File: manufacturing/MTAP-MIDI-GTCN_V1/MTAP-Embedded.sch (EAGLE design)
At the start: 61 parts, among them J1 629105150521, X10 0R, X11 0R

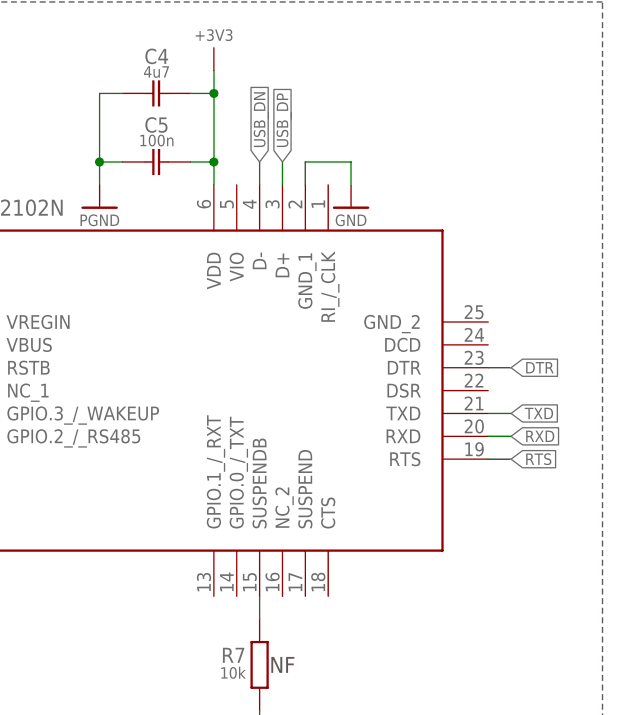
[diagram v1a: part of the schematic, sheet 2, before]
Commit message: Finalised Board
added missing connections to USB Bridge.
Added 3d Images to docs
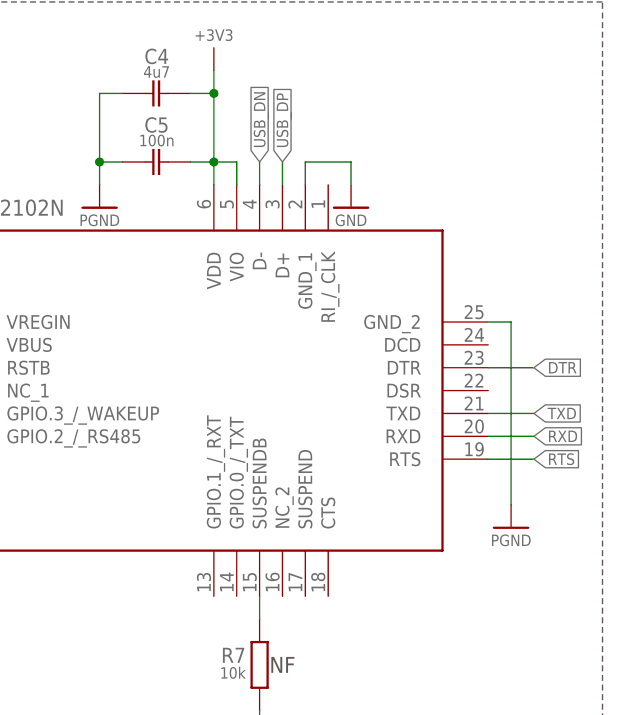
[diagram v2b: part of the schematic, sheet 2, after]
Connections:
- net +3V3: now also D2.VIO
- net PGND: now also D2.GND_2
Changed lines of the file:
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@@
 <part name="SPI_CLK" library="solpad_GruS" library_urn="urn:adsk.eagle:library:13571267" deviceset="SMD-TP" device="" package3d_urn="urn:adsk.eagle:package:38312116/4"/>
 <part name="S1" library="switch_GruS" library_urn="urn:adsk.eagle:library:13571161" deviceset="TASTE10XX" device="WE" package3d_urn="urn:adsk.eagle:package:18368072/4" value="BOOT"/>
+<part name="PGND5" library="supply_GruS" library_urn="urn:adsk.eagle:library:13579815" deviceset="PGND" device=""/>
 </parts>
 <sheets>
@@
 <attribute name="VALUE" x="78.74" y="91.44" size="1.27" layer="96" font="vector" align="bottom-center"/>
 </instance>
+<instance part="PGND5" gate="G$1" x="162.56" y="208.28" smashed="yes">
+<attribute name="VALUE" x="162.56" y="206.248" size="1.27" layer="96" font="vector" align="bottom-center"/>
+</instance>
 </instances>
 <busses>
@@
 </segment>
 <segment>
+<pinref part="GND1" gate="1" pin="GND"/>
+<wire x1="144.78" y1="248.92" x2="144.78" y2="246.38" width="0.1524" layer="91"/>
+<wire x1="139.7" y1="248.92" x2="144.78" y2="248.92" width="0.1524" layer="91"/>
 <wire x1="139.7" y1="246.38" x2="139.7" y2="248.92" width="0.1524" layer="91"/>
-<wire x1="139.7" y1="248.92" x2="144.78" y2="248.92" width="0.1524" layer="91"/>
-<wire x1="144.78" y1="248.92" x2="144.78" y2="246.38" width="0.1524" layer="91"/>
-<pinref part="GND1" gate="1" pin="GND"/>
 <pinref part="D2" gate="G$1" pin="GND_1"/>
 </segment>
@@
 </segment>
 <segment>
-<wire x1="160.02" y1="220.98" x2="162.56" y2="220.98" width="0.1524" layer="91"/>
-<label x="162.56" y="220.98" size="1.27" layer="95" xref="yes"/>
+<wire x1="160.02" y1="220.98" x2="165.1" y2="220.98" width="0.1524" layer="91"/>
+<label x="165.1" y="220.98" size="1.27" layer="95" xref="yes"/>
 <pinref part="D2" gate="G$1" pin="TXD"/>
 </segment>
@@
 </segment>
 <segment>
-<wire x1="160.02" y1="218.44" x2="162.56" y2="218.44" width="0.1524" layer="91"/>
-<label x="162.56" y="218.44" size="1.27" layer="95" xref="yes"/>
+<wire x1="160.02" y1="218.44" x2="165.1" y2="218.44" width="0.1524" layer="91"/>
+<label x="165.1" y="218.44" size="1.27" layer="95" xref="yes"/>
 <pinref part="D2" gate="G$1" pin="RXD"/>
 </segment>
@@
 </segment>
 <segment>
-<wire x1="160.02" y1="226.06" x2="162.56" y2="226.06" width="0.1524" layer="91"/>
-<label x="162.56" y="226.06" size="1.27" layer="95" xref="yes"/>
+<wire x1="160.02" y1="226.06" x2="165.1" y2="226.06" width="0.1524" layer="91"/>
+<label x="165.1" y="226.06" size="1.27" layer="95" xref="yes"/>
 <pinref part="D2" gate="G$1" pin="DTR"/>
 </segment>
@@
 </segment>
 <segment>
-<wire x1="160.02" y1="215.9" x2="162.56" y2="215.9" width="0.1524" layer="91"/>
-<label x="162.56" y="215.9" size="1.27" layer="95" xref="yes"/>
+<wire x1="160.02" y1="215.9" x2="165.1" y2="215.9" width="0.1524" layer="91"/>
+<label x="165.1" y="215.9" size="1.27" layer="95" xref="yes"/>
 <pinref part="D2" gate="G$1" pin="RTS"/>
 </segment>
@@
 <wire x1="129.54" y1="259.08" x2="129.54" y2="256.54" width="0.1524" layer="91"/>
 <junction x="129.54" y="256.54"/>
+<pinref part="D2" gate="G$1" pin="VIO"/>
+<wire x1="132.08" y1="246.38" x2="132.08" y2="248.92" width="0.1524" layer="91"/>
+<wire x1="132.08" y1="248.92" x2="129.54" y2="248.92" width="0.1524" layer="91"/>
 </segment>
 </net>
@@
 <junction x="116.84" y="248.92"/>
 </segment>
-</net>
+<segment>
+<pinref part="D2" gate="G$1" pin="GND_2"/>
+<wire x1="160.02" y1="231.14" x2="162.56" y2="231.14" width="0.1524" layer="91"/>
+<wire x1="162.56" y1="231.14" x2="162.56" y2="210.82" width="0.1524" layer="91"/>
+<pinref part="PGND5" gate="G$1" pin="PGND"/>
+</segment>
+</net>

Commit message: midi functional test
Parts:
- added C19: 1u, rcl_GruS:C-EUC0805
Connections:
- net AGND: now also C19.2
- net AINP: now also C19.1, D1.IO4
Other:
- note added: "G6 Filter (~1500Hz) 2.8V/V Gain Sallen Key Aufbau Butterworth Charakeristik Single Supply"
- note removed: "A6 Filter (1760Hz) 2V/V Gain Sallen Key Aufbau Butterworth Charakeristik Single Supply"
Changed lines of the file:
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@@
 <part name="S1" library="switch_GruS" library_urn="urn:adsk.eagle:library:13571161" deviceset="TASTE10XX" device="WE" package3d_urn="urn:adsk.eagle:package:18368072/4" value="BOOT"/>
 <part name="PGND5" library="supply_GruS" library_urn="urn:adsk.eagle:library:13579815" deviceset="PGND" device=""/>
+<part name="C19" library="rcl_GruS" library_urn="urn:adsk.eagle:library:13572313" deviceset="C-EU" device="C0805" package3d_urn="urn:adsk.eagle:package:23617/2" value="1u"/>
+<part name="AGND13" library="supply_GruS" library_urn="urn:adsk.eagle:library:13579815" deviceset="AGND" device=""/>
 </parts>
 <sheets>
@@
 <instance part="SPIQ" gate="G$1" x="114.3" y="114.3" smashed="yes"/>
 <instance part="SPI_CLK" gate="G$1" x="119.38" y="114.3" smashed="yes"/>
+<instance part="C19" gate="G$1" x="129.54" y="157.48" smashed="yes">
+<attribute name="NAME" x="128.778" y="156.9466" size="1.6764" layer="95" font="vector" align="bottom-right"/>
+<attribute name="VALUE" x="128.524" y="154.1526" size="1.27" layer="96" font="vector" align="bottom-right"/>
+</instance>
+<instance part="AGND13" gate="G$1" x="129.54" y="147.32" smashed="yes">
+<attribute name="VALUE" x="129.54" y="145.288" size="1.27" layer="96" font="vector" align="bottom-center"/>
+</instance>
 </instances>
 <busses>
@@
 <pinref part="D1" gate="G$1" pin="GND_1"/>
 <wire x1="81.28" y1="210.82" x2="83.82" y2="210.82" width="0.1524" layer="91"/>
+</segment>
+<segment>
+<pinref part="GND8" gate="1" pin="GND"/>
+<pinref part="C3" gate="G$1" pin="2"/>
+<wire x1="55.88" y1="149.86" x2="55.88" y2="152.4" width="0.1524" layer="91"/>
 </segment>
 <segment>
@@
 <pinref part="GND7" gate="1" pin="GND"/>
 </segment>
-<segment>
-<pinref part="GND8" gate="1" pin="GND"/>
-<pinref part="C3" gate="G$1" pin="2"/>
-<wire x1="55.88" y1="149.86" x2="55.88" y2="152.4" width="0.1524" layer="91"/>
-</segment>
 </net>
 <net name="GPIO0" class="0">
 <segment>
 <pinref part="D1" gate="G$1" pin="IO0"/>
-<wire x1="121.92" y1="210.82" x2="124.46" y2="210.82" width="0.1524" layer="91"/>
-<label x="124.46" y="210.82" size="1.27" layer="95" xref="yes"/>
+<wire x1="121.92" y1="210.82" x2="127" y2="210.82" width="0.1524" layer="91"/>
+<label x="127" y="210.82" size="1.27" layer="95" xref="yes"/>
 </segment>
 </net>
@@
 <segment>
 <pinref part="D1" gate="G$1" pin="TXD0"/>
-<wire x1="121.92" y1="185.42" x2="124.46" y2="185.42" width="0.1524" layer="91"/>
-<label x="124.46" y="185.42" size="1.27" layer="95" xref="yes"/>
+<wire x1="121.92" y1="185.42" x2="127" y2="185.42" width="0.1524" layer="91"/>
+<label x="127" y="185.42" size="1.27" layer="95" xref="yes"/>
 </segment>
 </net>
@@
 <segment>
 <pinref part="D1" gate="G$1" pin="RXD0"/>
-<wire x1="121.92" y1="187.96" x2="124.46" y2="187.96" width="0.1524" layer="91"/>
-<label x="124.46" y="187.96" size="1.27" layer="95" xref="yes"/>
+<wire x1="121.92" y1="187.96" x2="127" y2="187.96" width="0.1524" layer="91"/>
+<label x="127" y="187.96" size="1.27" layer="95" xref="yes"/>
 </segment>
 </net>
@@
 <segment>
 <pinref part="D1" gate="G$1" pin="IO5"/>
-<wire x1="121.92" y1="200.66" x2="124.46" y2="200.66" width="0.1524" layer="91"/>
-<label x="124.46" y="200.66" size="1.27" layer="95" xref="yes"/>
+<wire x1="121.92" y1="200.66" x2="127" y2="200.66" width="0.1524" layer="91"/>
+<label x="127" y="200.66" size="1.27" layer="95" xref="yes"/>
 </segment>
 <segment>
@@
 <segment>
 <pinref part="D1" gate="G$1" pin="IO18"/>
-<wire x1="121.92" y1="198.12" x2="124.46" y2="198.12" width="0.1524" layer="91"/>
-<label x="124.46" y="198.12" size="1.27" layer="95" xref="yes"/>
+<wire x1="121.92" y1="198.12" x2="127" y2="198.12" width="0.1524" layer="91"/>
+<label x="127" y="198.12" size="1.27" layer="95" xref="yes"/>
 </segment>
 <segment>
@@
 <segment>
 <pinref part="D1" gate="G$1" pin="IO19"/>
-<wire x1="121.92" y1="195.58" x2="124.46" y2="195.58" width="0.1524" layer="91"/>
-<label x="124.46" y="195.58" size="1.27" layer="95" xref="yes"/>
+<wire x1="121.92" y1="195.58" x2="127" y2="195.58" width="0.1524" layer="91"/>
+<label x="127" y="195.58" size="1.27" layer="95" xref="yes"/>
 </segment>
 <segment>
@@
 <wire x1="73.66" y1="111.76" x2="73.66" y2="109.22" width="0.1524" layer="91"/>
 </segment>
+<segment>
+<pinref part="C19" gate="G$1" pin="2"/>
+<wire x1="129.54" y1="149.86" x2="129.54" y2="152.4" width="0.1524" layer="91"/>
+<pinref part="AGND13" gate="G$1" pin="AGND"/>
+</segment>
 </net>
 <net name="AINP" class="0">
@@
 <pinref part="POST-AFE" gate="G$1" pin="P$1"/>
 <wire x1="93.98" y1="111.76" x2="93.98" y2="109.22" width="0.1524" layer="91"/>
+</segment>
+<segment>
+<pinref part="C19" gate="G$1" pin="1"/>
+<wire x1="129.54" y1="160.02" x2="129.54" y2="180.34" width="0.1524" layer="91"/>
+<pinref part="D1" gate="G$1" pin="IO4"/>
+<wire x1="127" y1="208.28" x2="124.46" y2="208.28" width="0.1524" layer="91"/>
+<label x="127" y="208.28" size="1.27" layer="95" xref="yes"/>
+<wire x1="124.46" y1="208.28" x2="121.92" y2="208.28" width="0.1524" layer="91"/>
+<wire x1="129.54" y1="180.34" x2="124.46" y2="180.34" width="0.1524" layer="91"/>
+<wire x1="124.46" y1="180.34" x2="124.46" y2="208.28" width="0.1524" layer="91"/>
+<junction x="124.46" y="208.28"/>
 </segment>
 </net>
@@
 Supply and Reference</text>
 <text x="88.9" y="172.72" size="2.54" layer="97" font="vector" align="bottom-center">Low Pass Filter</text>
-<text x="162.56" y="116.84" size="1.778" layer="97" font="vector" rot="R180">A6 Filter (1760Hz)
-2V/V Gain
+<text x="162.56" y="116.84" size="1.778" layer="97" font="vector" rot="R180">G6 Filter (~1500Hz)
+2.8V/V Gain
 Sallen Key Aufbau
 Butterworth Charakeristik

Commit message: upd midi serial
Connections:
- new net MTDO: D1.IO15
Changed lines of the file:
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@@
+</segment>
+</net>
+<net name="MTDO" class="0">
+<segment>
+<pinref part="D1" gate="G$1" pin="IO15"/>
+<wire x1="83.82" y1="154.94" x2="78.74" y2="154.94" width="0.1524" layer="91"/>
+<label x="78.74" y="154.94" size="1.27" layer="95" rot="R180" xref="yes"/>
 </segment>
 </net>

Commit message: placed pcb order
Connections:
- net +3V3: now also N1.NC
- net GND: no longer D2.GND_1
- net PGND: now also D2.GND_1
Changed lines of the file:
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@@
 <part name="N2" library="opv_GruS" library_urn="urn:adsk.eagle:library:27826080" deviceset="TLV271C*" device="DBVTG4" package3d_urn="urn:adsk.eagle:package:38237664/3" value="TLV271G4"/>
 <part name="D2" library="ic_GruS" library_urn="urn:adsk.eagle:library:13571010" deviceset="CP2102N-A02-GQFN24" device="" package3d_urn="urn:adsk.eagle:package:38290199/3" value="CP2102N"/>
-<part name="GND1" library="supply_GruS" library_urn="urn:adsk.eagle:library:13579815" deviceset="GND" device=""/>
 <part name="+3V1" library="supply_GruS" library_urn="urn:adsk.eagle:library:13579815" deviceset="+3V3" device=""/>
 <part name="C5" library="rcl_GruS" library_urn="urn:adsk.eagle:library:13572313" deviceset="C-EU" device="C0805" package3d_urn="urn:adsk.eagle:package:23617/2" value="100n"/>
@@
 <part name="C19" library="rcl_GruS" library_urn="urn:adsk.eagle:library:13572313" deviceset="C-EU" device="C0805" package3d_urn="urn:adsk.eagle:package:23617/2" value="1u"/>
 <part name="AGND13" library="supply_GruS" library_urn="urn:adsk.eagle:library:13579815" deviceset="AGND" device=""/>
+<part name="+3V8" library="supply_GruS" library_urn="urn:adsk.eagle:library:13579815" deviceset="+3V3" device=""/>
+<part name="PGND18" library="supply_GruS" library_urn="urn:adsk.eagle:library:13579815" deviceset="PGND" device=""/>
 </parts>
 <sheets>
@@
 <attribute name="VALUE" x="102.87" y="243.84" size="1.778" layer="96" align="center-left"/>
 </instance>
-<instance part="GND1" gate="1" x="144.78" y="243.84" smashed="yes">
-<attribute name="VALUE" x="144.78" y="241.808" size="1.27" layer="96" font="vector" align="bottom-center"/>
-</instance>
 <instance part="+3V1" gate="G$1" x="129.54" y="261.62" smashed="yes">
 <attribute name="VALUE" x="129.54" y="262.382" size="1.27" layer="96" font="vector" align="bottom-center"/>
@@
 <instance part="PGND5" gate="G$1" x="162.56" y="208.28" smashed="yes">
 <attribute name="VALUE" x="162.56" y="206.248" size="1.27" layer="96" font="vector" align="bottom-center"/>
+</instance>
+<instance part="+3V8" gate="G$1" x="101.6" y="157.48" smashed="yes">
+<attribute name="VALUE" x="101.6" y="158.242" size="1.27" layer="96" font="vector" align="bottom-center"/>
+</instance>
+<instance part="PGND18" gate="G$1" x="144.78" y="243.84" smashed="yes">
+<attribute name="VALUE" x="144.78" y="241.808" size="1.27" layer="96" font="vector" align="bottom-center"/>
 </instance>
 </instances>
@@
 <wire x1="139.7" y1="91.44" x2="139.7" y2="81.28" width="0.1524" layer="91"/>
 <pinref part="GND2" gate="1" pin="GND"/>
-</segment>
-<segment>
-<pinref part="GND1" gate="1" pin="GND"/>
-<wire x1="144.78" y1="248.92" x2="144.78" y2="246.38" width="0.1524" layer="91"/>
-<wire x1="139.7" y1="248.92" x2="144.78" y2="248.92" width="0.1524" layer="91"/>
-<wire x1="139.7" y1="246.38" x2="139.7" y2="248.92" width="0.1524" layer="91"/>
-<pinref part="D2" gate="G$1" pin="GND_1"/>
 </segment>
 </net>
@@
 <pinref part="V2" gate="G$1" pin="E"/>
 <wire x1="58.42" y1="208.28" x2="58.42" y2="210.82" width="0.1524" layer="91"/>
-<wire x1="58.42" y1="210.82" x2="33.02" y2="210.82" width="0.1524" layer="91"/>
-<wire x1="33.02" y1="210.82" x2="33.02" y2="220.98" width="0.1524" layer="91"/>
+<wire x1="58.42" y1="210.82" x2="43.18" y2="210.82" width="0.1524" layer="91"/>
 <pinref part="R4" gate="G$1" pin="1"/>
-<wire x1="33.02" y1="220.98" x2="38.1" y2="220.98" width="0.1524" layer="91"/>
-<wire x1="33.02" y1="220.98" x2="30.48" y2="220.98" width="0.1524" layer="91"/>
-<junction x="33.02" y="220.98"/>
-<label x="30.48" y="220.98" size="1.27" layer="95" font="vector" rot="R180" xref="yes"/>
+<wire x1="35.56" y1="220.98" x2="38.1" y2="220.98" width="0.1524" layer="91"/>
+<wire x1="35.56" y1="220.98" x2="33.02" y2="220.98" width="0.1524" layer="91"/>
+<label x="33.02" y="220.98" size="1.27" layer="95" font="vector" rot="R180" xref="yes"/>
+<wire x1="35.56" y1="220.98" x2="35.56" y2="218.44" width="0.1524" layer="91"/>
+<junction x="35.56" y="220.98"/>
+<wire x1="35.56" y1="218.44" x2="43.18" y2="210.82" width="0.1524" layer="91"/>
 </segment>
 <segment>
@@
 <pinref part="V1" gate="G$1" pin="E"/>
 <wire x1="58.42" y1="215.9" x2="58.42" y2="213.36" width="0.1524" layer="91"/>
-<wire x1="58.42" y1="213.36" x2="35.56" y2="213.36" width="0.1524" layer="91"/>
+<wire x1="58.42" y1="213.36" x2="43.18" y2="213.36" width="0.1524" layer="91"/>
 <pinref part="R6" gate="G$1" pin="1"/>
-<wire x1="35.56" y1="213.36" x2="35.56" y2="203.2" width="0.1524" layer="91"/>
-<wire x1="35.56" y1="203.2" x2="38.1" y2="203.2" width="0.1524" layer="91"/>
-<wire x1="35.56" y1="203.2" x2="30.48" y2="203.2" width="0.1524" layer="91"/>
+<wire x1="38.1" y1="203.2" x2="35.56" y2="203.2" width="0.1524" layer="91"/>
+<label x="33.02" y="203.2" size="1.27" layer="95" font="vector" rot="R180" xref="yes"/>
+<wire x1="35.56" y1="203.2" x2="33.02" y2="203.2" width="0.1524" layer="91"/>
+<wire x1="35.56" y1="203.2" x2="35.56" y2="205.74" width="0.1524" layer="91"/>
 <junction x="35.56" y="203.2"/>
-<label x="30.48" y="203.2" size="1.27" layer="95" font="vector" rot="R180" xref="yes"/>
+<wire x1="35.56" y1="205.74" x2="43.18" y2="213.36" width="0.1524" layer="91"/>
 </segment>
 <segment>
@@
 <wire x1="132.08" y1="248.92" x2="129.54" y2="248.92" width="0.1524" layer="91"/>
 </segment>
+<segment>
+<pinref part="N1" gate="G$1" pin="NC"/>
+<wire x1="99.06" y1="152.4" x2="101.6" y2="152.4" width="0.1524" layer="91"/>
+<pinref part="+3V8" gate="G$1" pin="+3V3"/>
+<wire x1="101.6" y1="152.4" x2="101.6" y2="154.94" width="0.1524" layer="91"/>
+</segment>
 </net>
 <net name="PGND" class="0">
@@
 <pinref part="PGND5" gate="G$1" pin="PGND"/>
 </segment>
-</net>
+<segment>
+<wire x1="144.78" y1="248.92" x2="144.78" y2="246.38" width="0.1524" layer="91"/>
+<wire x1="139.7" y1="248.92" x2="144.78" y2="248.92" width="0.1524" layer="91"/>
+<wire x1="139.7" y1="246.38" x2="139.7" y2="248.92" width="0.1524" layer="91"/>
+<pinref part="D2" gate="G$1" pin="GND_1"/>
+<pinref part="PGND18" gate="G$1" pin="PGND"/>
+</segment>
+</net>
